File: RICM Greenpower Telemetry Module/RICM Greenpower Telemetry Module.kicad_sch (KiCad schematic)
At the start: 35 parts, among them J1 Conn_01x02_Female, J10 Conn_01x02_Female, J2 Conn_01x02_Female, J3 Conn_01x02_Female, J4 Jack-DC, J5 Conn_01x05_Female, J6 Conn_02x04_Counter_Clockwise, J7 Conn_01x03_Female, J8 Conn_01x03_Female, J9 Conn_01x04_Female, U1 Pico, U2 MPU_6050_module, U3 Adafruit_MicroSD_SPI_SDIO, U4 LTC2990

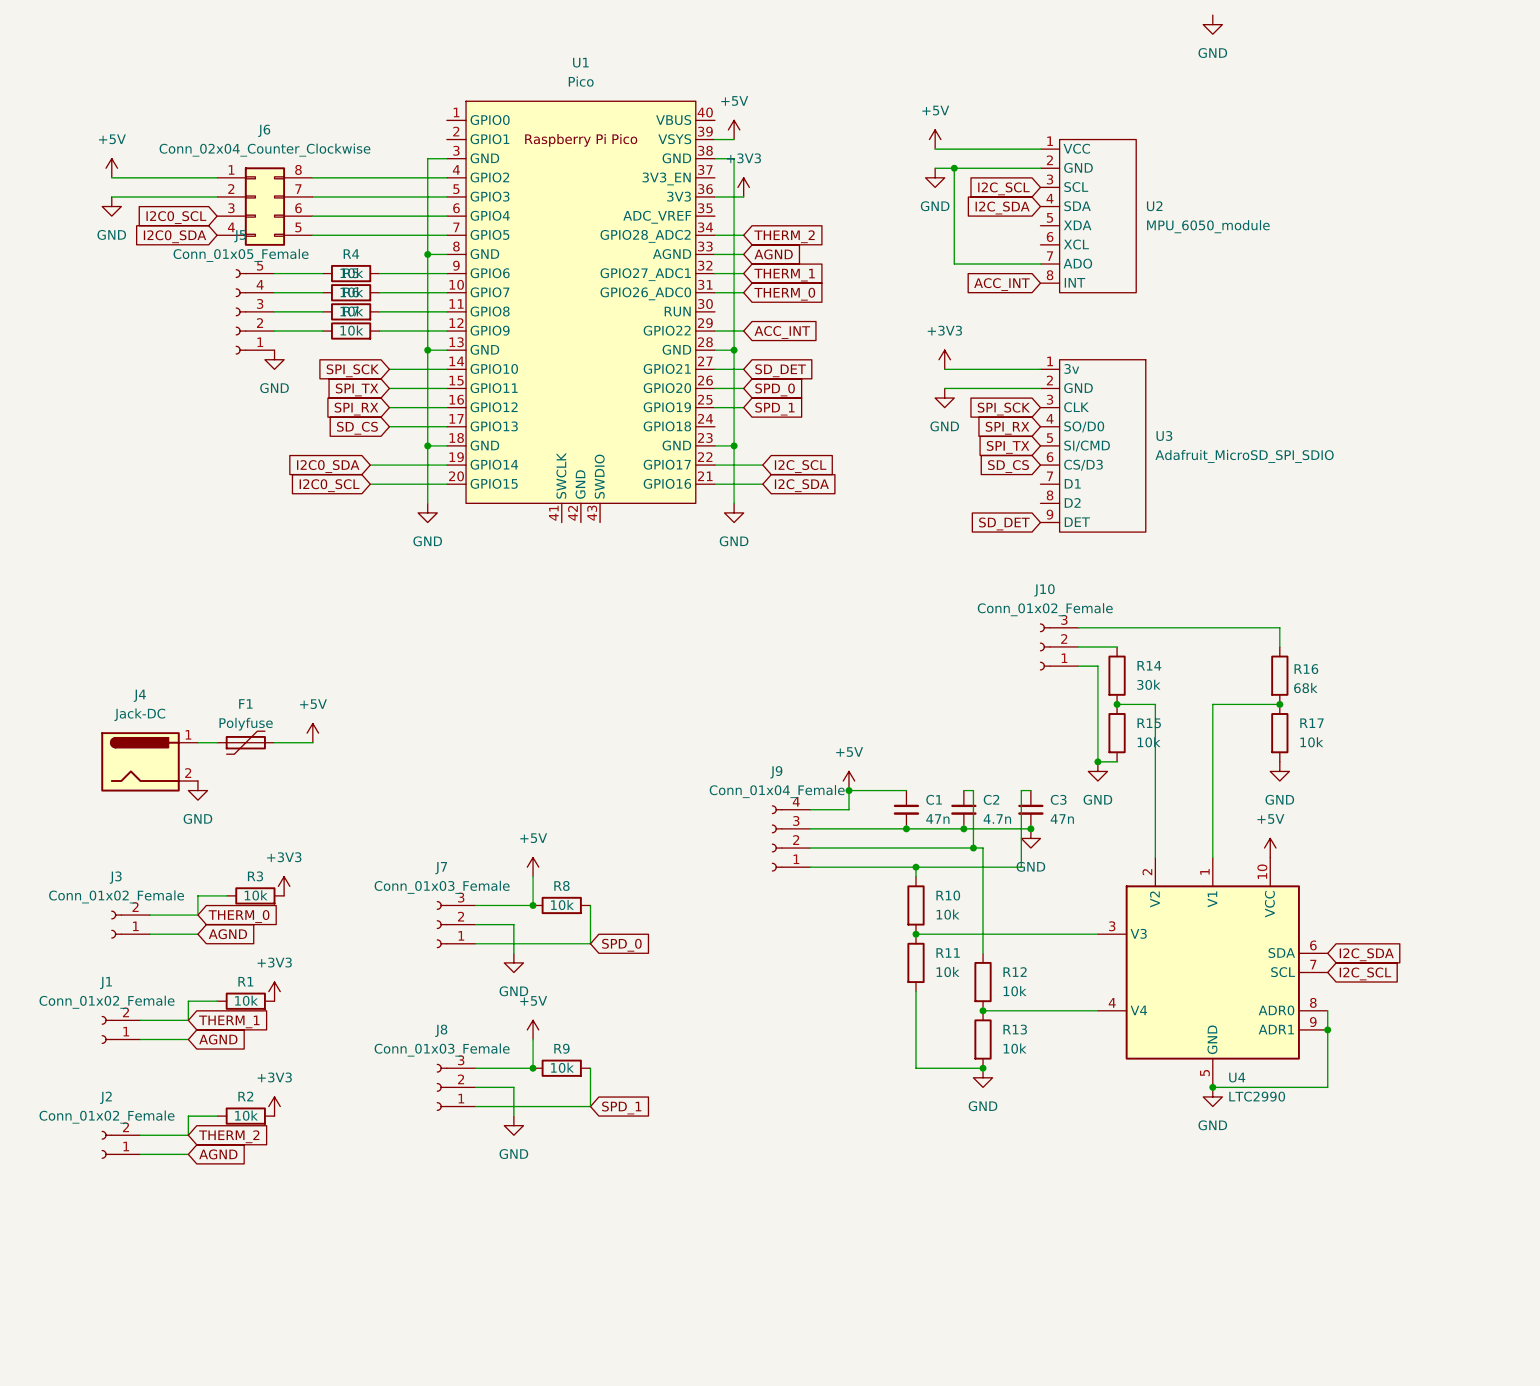
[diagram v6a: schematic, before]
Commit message: added onboard regulator
Added onboard regulator and associated components. Added 4th thermistor connector.
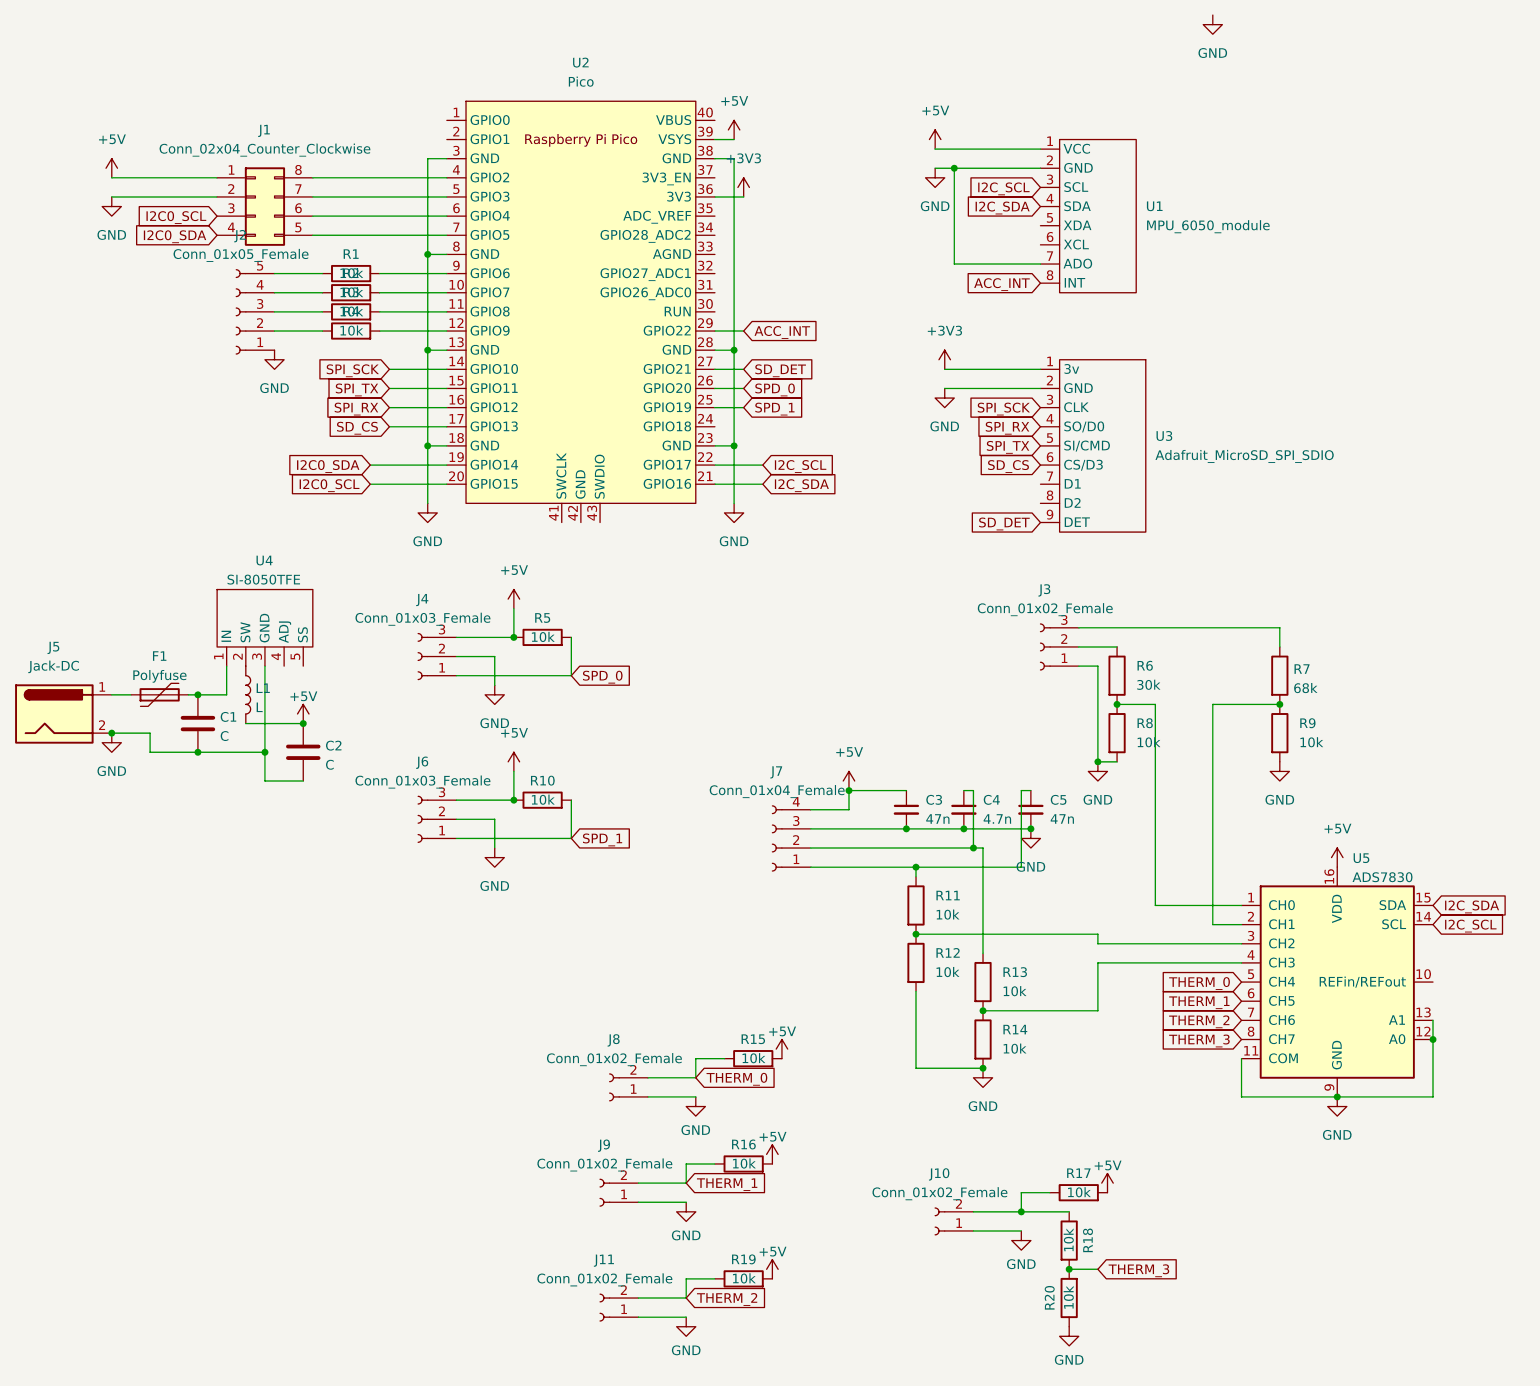
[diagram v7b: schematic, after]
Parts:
- removed U4: LTC2990, Package_SO:MSOP-10_3x3mm_P0.5mm, symbol Sensor:LTC2990
- added C1, C2: C, Capacitor_THT:CP_Radial_D8.0mm_P3.50mm, symbol Device:C
- added J10: Conn_01x02_Female, Connector_PinHeader_2.54mm:PinHeader_1x02_P2.54mm_Vertical, symbol Connector:Conn_01x02_Female
- added L1: L, Inductor_THT:L_Axial_L6.6mm_D2.7mm_P10.16mm_Horizontal_Vishay_IM-2, symbol Device:L
- added R17, R18, R20: 10k, Resistor_THT:R_Axial_DIN0207_L6.3mm_D2.5mm_P7.62mm_Horizontal, symbol Device:R
- added U4: SI-8050TFE, Package_TO_SOT_THT:TO-220-5_P3.4x3.7mm_StaggerOdd_Lead3.8mm_Vertical, symbol Regulator_Switching:SI-8050TFE
- added U5: ADS7830, Package_SO:TSSOP-16_4.4x5mm_P0.65mm, symbol Analog_DAC:ADS7830
- renumbered C1 to C3, C2 to C4, C3 to C5, J6 to J1, J2 to J11, J5 to J2, J10 to J3, J7 to J4, J4 to J5, J8 to J6, J9 to J7, J3 to J8, J1 to J9, R4 to R1, R9 to R10, R10 to R11, R11 to R12, R12 to R13, R13 to R14, R3 to R15, R1 to R16, R2 to R19, R5 to R2, R6 to R3, R7 to R4, R8 to R5, R14 to R6, R16 to R7, R15 to R8, R17 to R9, U2 to U1, U1 to U2
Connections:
- net +3V3: no longer R15.2, R16.2, R19.2
- net +5V: now also R15.2, R16.2, R19.2, C2.2, L1.2, R17.2, U5.16 (VDD); no longer F1.2
- net GND: now also J11.1 (Pin_1), J8.1 (Pin_1), J9.1 (Pin_1), C1.2, C2.1, J10.1 (Pin_1), R20.1, U4.3 (GND), U5.11 (COM), U5.12 (A0), U5.13 (A1), U5.9 (GND)
- net I2C_SCL: now also U5.14 (SCL)
- net I2C_SDA: now also U5.15 (SDA)
- net THERM_0: now also U5.5 (CH4); no longer U2.31 (GPIO26_ADC0)
- net THERM_1: now also U5.6 (CH5); no longer U2.32 (GPIO27_ADC1)
- net THERM_2: now also U5.7 (CH6); no longer U2.34 (GPIO28_ADC2)
- net at R7.2, R9.1: now also U5.2 (CH1)
- net at R6.2, R8.1: now also U5.1 (CH0)
- net at R11.2, R12.1: now also U5.3 (CH2)
- net at R13.2, R14.1: now also U5.4 (CH3)
- removed net AGND: J11.1 (Pin_1), J8.1 (Pin_1), J9.1 (Pin_1), U2.33 (AGND)
- new net: C1.1, F1.2, U4.1 (IN)
- new net: J10.2 (Pin_2), R17.1, R18.1
- new net: L1.1, U4.2 (SW)
- new net THERM_3: R18.2, R20.2, U5.8 (CH7)
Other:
- moved on the sheet: F1, J11, J4, J5, J6, J8, J9, R10, R15, R16, R19, R5
